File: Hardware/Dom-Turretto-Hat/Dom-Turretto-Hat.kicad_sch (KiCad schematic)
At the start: 12 parts, among them J1 Raspberry_Pi_2_3, U1 CAT24C32WI-GT3

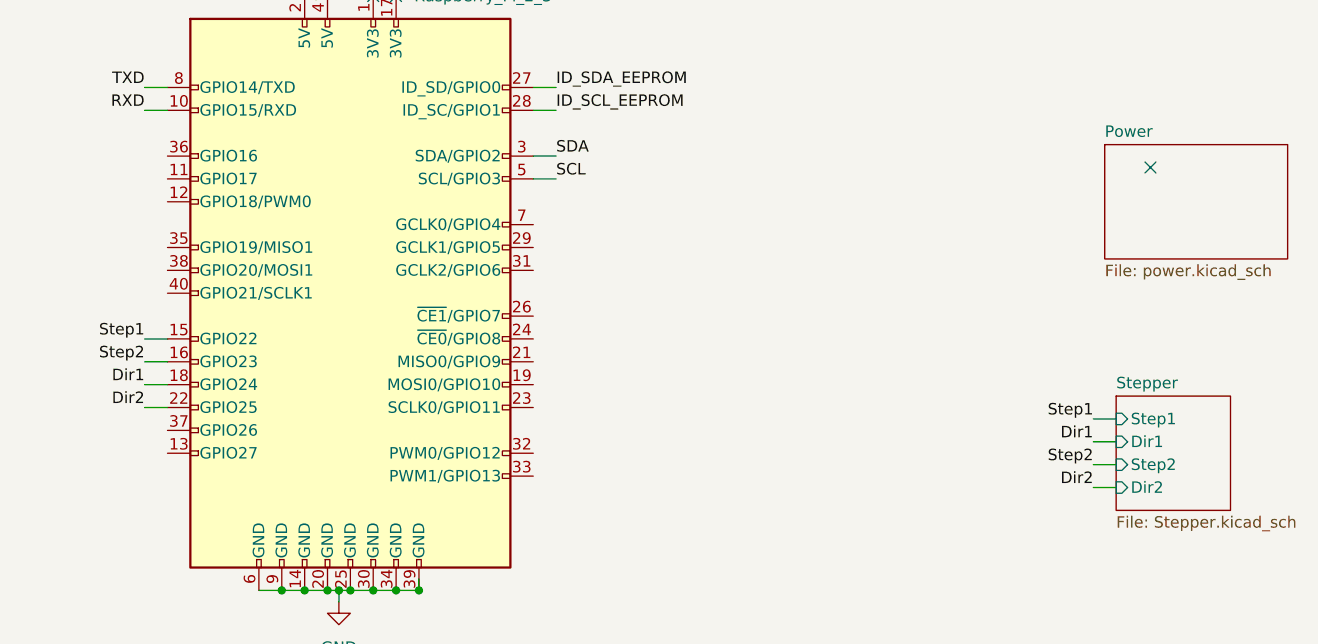
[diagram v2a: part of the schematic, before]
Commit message: Fix power circuitry values
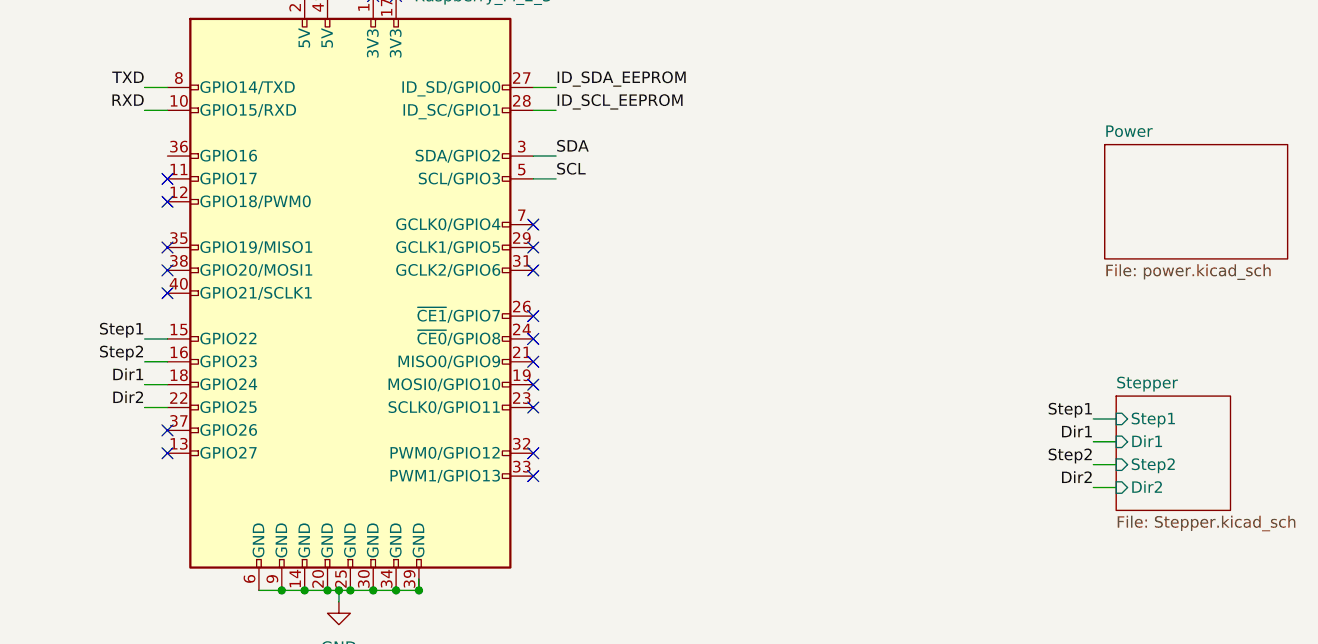
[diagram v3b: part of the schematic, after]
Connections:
- no-connect marks 4 -> 20
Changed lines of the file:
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@@
   (no_connect (at 146.05 69.85))
   (no_connect (at 148.59 69.85))
+  (no_connect (at 123.19 90.17))
+  (no_connect (at 123.19 100.33))
+  (no_connect (at 123.19 97.79))
+  (no_connect (at 123.19 92.71))
+  (no_connect (at 163.83 95.25))
+  (no_connect (at 163.83 97.79))
+  (no_connect (at 163.83 100.33))
+  (no_connect (at 163.83 105.41))
+  (no_connect (at 163.83 107.95))
+  (no_connect (at 163.83 110.49))
+  (no_connect (at 163.83 113.03))
+  (no_connect (at 163.83 115.57))
+  (no_connect (at 163.83 120.65))
+  (no_connect (at 163.83 123.19))
+  (no_connect (at 123.19 102.87))
+  (no_connect (at 123.19 120.65))
+  (no_connect (at 123.19 118.11))
   (no_connect (at -303.53 -21.59))
-  (no_connect (at 232.41 88.9))
   (wire (pts (xy 52.07 105.41) (xy 52.07 107.95))
     (stroke (width 0) (type default) (color 0 0 0 0))
@@
       (reference "#PWR013") (unit 1) (value "VCC") (footprint "")
     )
-    (path "/12e93b0c-a239-457f-b141-0c3b73a9b90a/4ae1d417-485a-437f-8fe9-cf7ad21c0f01"
-      (reference "#PWR014") (unit 1) (value "GND") (footprint "")
-    )
     (path "/12e93b0c-a239-457f-b141-0c3b73a9b90a/3dfc33ce-2f23-4a0c-8f41-0134d6c7a2a4"
       (reference "#PWR015") (unit 1) (value "GND") (footprint "")
@@
       (reference "#PWR021") (unit 1) (value "GND") (footprint "")
     )
-    (path "/12e93b0c-a239-457f-b141-0c3b73a9b90a/edde2f9a-acc0-48b1-bb93-b02152a9c39d"
-      (reference "#PWR026") (unit 1) (value "VCC") (footprint "")
-    )
     (path "/12e93b0c-a239-457f-b141-0c3b73a9b90a/23a39806-5bcf-46b3-9dd9-56270df61814"
       (reference "#PWR027") (unit 1) (value "GND") (footprint "")
@@
       (reference "#PWR0102") (unit 1) (value "GND") (footprint "")
     )
-    (path "/28fd1fbc-026b-4dd2-b303-4aef81adb474/a67e1f19-66f8-4d89-a414-1dd966045ad0"
-      (reference "#PWR0103") (unit 1) (value "+5V") (footprint "")
-    )
-    (path "/28fd1fbc-026b-4dd2-b303-4aef81adb474/9dc995cd-8c94-45d3-a4e1-d727a2822c72"
-      (reference "#PWR0104") (unit 1) (value "+5V") (footprint "")
-    )
-    (path "/28fd1fbc-026b-4dd2-b303-4aef81adb474/26251c45-5edc-47f5-bbe9-a3fa40eb07cf"
-      (reference "#PWR0105") (unit 1) (value "+5V") (footprint "")
-    )
-    (path "/28fd1fbc-026b-4dd2-b303-4aef81adb474/b601569f-09f4-4cef-b542-0b3745596966"
-      (reference "#PWR0106") (unit 1) (value "+5V") (footprint "")
-    )
-    (path "/28fd1fbc-026b-4dd2-b303-4aef81adb474/a83d4d91-ae71-431a-9357-40ec7588a902"
-      (reference "#PWR0107") (unit 1) (value "+5V") (footprint "")
-    )
-    (path "/28fd1fbc-026b-4dd2-b303-4aef81adb474/6788054c-34eb-4edd-af0a-8aff4765f859"
-      (reference "#PWR0108") (unit 1) (value "+5V") (footprint "")
-    )
-    (path "/28fd1fbc-026b-4dd2-b303-4aef81adb474/e9bf3fe6-e1cc-4b8d-bbb8-700e183aad7b"
-      (reference "#PWR0109") (unit 1) (value "+5V") (footprint "")
-    )
-    (path "/28fd1fbc-026b-4dd2-b303-4aef81adb474/35f07658-fb63-46ec-8bc3-dc98eda80c44"
-      (reference "#PWR0110") (unit 1) (value "+5V") (footprint "")
+    (path "/28fd1fbc-026b-4dd2-b303-4aef81adb474/c26481a5-551f-455c-a702-bce8abb1fe4e"
+      (reference "#PWR0103") (unit 1) (value "+3V3") (footprint "")
+    )
+    (path "/28fd1fbc-026b-4dd2-b303-4aef81adb474/7b37127e-e11c-4058-9b9e-3ba186a4a412"
+      (reference "#PWR0104") (unit 1) (value "+3V3") (footprint "")
+    )
+    (path "/28fd1fbc-026b-4dd2-b303-4aef81adb474/539ce550-73e1-4bff-bfe2-8c24d3e902a4"
+      (reference "#PWR0105") (unit 1) (value "+3V3") (footprint "")
+    )
+    (path "/28fd1fbc-026b-4dd2-b303-4aef81adb474/ae68f93a-eb13-4a21-940c-82130d925b20"
+      (reference "#PWR0106") (unit 1) (value "+3V3") (footprint "")
+    )
+    (path "/28fd1fbc-026b-4dd2-b303-4aef81adb474/3d9c11c1-d596-4401-a1a7-1c7f6241df8c"
+      (reference "#PWR0107") (unit 1) (value "+3V3") (footprint "")
+    )
+    (path "/28fd1fbc-026b-4dd2-b303-4aef81adb474/fa48996b-d3b8-4776-a72e-f75b7322c3d1"
+      (reference "#PWR0108") (unit 1) (value "+3V3") (footprint "")
+    )
+    (path "/28fd1fbc-026b-4dd2-b303-4aef81adb474/6521fb03-cbdb-41da-993d-d42db4a2d48a"
+      (reference "#PWR0109") (unit 1) (value "+3V3") (footprint "")
+    )
+    (path "/28fd1fbc-026b-4dd2-b303-4aef81adb474/5404de01-53f2-47e0-8e71-08810b932822"
+      (reference "#PWR0110") (unit 1) (value "+3V3") (footprint "")
+    )
+    (path "/12e93b0c-a239-457f-b141-0c3b73a9b90a/a639ca10-c811-4233-81c1-b214dc0c22a7"
+      (reference "#PWR0111") (unit 1) (value "GND") (footprint "")
     )
     (path "/28fd1fbc-026b-4dd2-b303-4aef81adb474/84977e32-dddb-4234-a567-e1e9c75d8f8b"
@@
       (reference "A2") (unit 1) (value "Pololu_Breakout_A4988") (footprint "Module:Pololu_Breakout-16_15.2x20.3mm")
     )
-    (path "/12e93b0c-a239-457f-b141-0c3b73a9b90a/ec276c8a-eb48-440f-b539-492777d28831"
-      (reference "C2") (unit 1) (value "22uF") (footprint "Capacitor_SMD:C_0603_1608Metric")
+    (path "/12e93b0c-a239-457f-b141-0c3b73a9b90a/4e526afd-8e77-485d-a370-3c86816ca539"
+      (reference "C1") (unit 1) (value "1uF") (footprint "Capacitor_SMD:C_0603_1608Metric")
+    )
+    (path "/12e93b0c-a239-457f-b141-0c3b73a9b90a/566f4d6a-3361-41fa-8a13-522c6df8e350"
+      (reference "C2") (unit 1) (value "10uF") (footprint "Capacitor_SMD:C_0603_1608Metric")
     )
     (path "/12e93b0c-a239-457f-b141-0c3b73a9b90a/ba2d8e02-8dff-41f2-94ab-2977ba7494f7"
-      (reference "C3") (unit 1) (value "6.8uF") (footprint "Capacitor_SMD:C_0603_1608Metric")
-    )
-    (path "/12e93b0c-a239-457f-b141-0c3b73a9b90a/881129b8-1053-44b9-bbe7-c43d6d8c66c3"
-      (reference "C4") (unit 1) (value "6.8uF") (footprint "Capacitor_SMD:C_0603_1608Metric")
+      (reference "C3") (unit 1) (value "10uF") (footprint "Capacitor_SMD:C_0603_1608Metric")
     )
     (path "/12e93b0c-a239-457f-b141-0c3b73a9b90a/f545c142-5d8e-40c4-b0fe-7c045a9cac0e"
@@
     )
     (path "/12e93b0c-a239-457f-b141-0c3b73a9b90a/70060f5d-b007-495f-a45f-7f1bfc4b8949"
-      (reference "C8") (unit 1) (value "180uF") (footprint "Capacitor_SMD:CP_Elec_8x11.9")
-    )
-    (path "/12e93b0c-a239-457f-b141-0c3b73a9b90a/24a04d23-1092-464e-96ea-d2d87b5f4b74"
-      (reference "C9") (unit 1) (value "10uF") (footprint "Capacitor_SMD:C_0603_1608Metric")
+      (reference "C8") (unit 1) (value "100uF") (footprint "Capacitor_SMD:CP_Elec_5x5.9")
     )
     (path "/12e93b0c-a239-457f-b141-0c3b73a9b90a/1e3bdcbd-8bf4-4d5f-8901-dadb4d9ff406"
@@
       (reference "C16") (unit 1) (value "47uF") (footprint "Capacitor_SMD:CP_Elec_6.3x7.7")
     )
-    (path "/12e93b0c-a239-457f-b141-0c3b73a9b90a/8a6cabaa-212f-4145-a004-b1da07d438ec"
-      (reference "D1") (unit 1) (value "D_Schottky") (footprint "Diode_SMD:D_SOD-123")
+    (path "/12e93b0c-a239-457f-b141-0c3b73a9b90a/b0d1c150-c935-43cc-9315-d503e1061c99"
+      (reference "C?") (unit 1) (value "47uF") (footprint "Capacitor_SMD:CP_Elec_6.3x7.7")
+    )
+    (path "/12e93b0c-a239-457f-b141-0c3b73a9b90a/23f8c4a1-bb0a-4aed-9a81-c18985f1140f"
+      (reference "D1") (unit 1) (value "DST1550S") (footprint "Package_TO_SOT_SMD:TO-277B")
     )
     (path "/12e93b0c-a239-457f-b141-0c3b73a9b90a/20d61a98-9d76-48c3-aea7-5d687e7dcd59"
@@
     )
     (path "/12e93b0c-a239-457f-b141-0c3b73a9b90a/89b193d6-28e4-4647-a3aa-6b8779163e05"
-      (reference "L2") (unit 1) (value "29uH") (footprint "Inductor_SMD:L_12x12mm_H8mm")
+      (reference "L2") (unit 1) (value "8.2uH") (footprint "iclr:Bourns_SRP1270")
     )
     (path "/12e93b0c-a239-457f-b141-0c3b73a9b90a/53065c22-5d58-4a1d-924c-019ba026a13b"
       (reference "PI_POW1") (unit 1) (value "LED") (footprint "LED_SMD:LED_0603_1608Metric")
     )
-    (path "/12e93b0c-a239-457f-b141-0c3b73a9b90a/87939eb2-1100-49c2-9486-7d16102560a9"
-      (reference "Q1") (unit 1) (value "RSJ250P10TL") (footprint "Package_TO_SOT_SMD:TO-263-3_TabPin2")
-    )
-    (path "/12e93b0c-a239-457f-b141-0c3b73a9b90a/d771511f-d16d-4f8b-8935-04481cf37b67"
-      (reference "Q2") (unit 1) (value "RSJ250P10TL") (footprint "Package_TO_SOT_SMD:TO-263-3_TabPin2")
+    (path "/12e93b0c-a239-457f-b141-0c3b73a9b90a/5a474f79-f8bc-4b50-af65-c0eaec3f07c2"
+      (reference "Q1") (unit 1) (value "SI4143DY-T1-GE3") (footprint "Package_SO:SOIC-8_3.9x4.9mm_P1.27mm")
+    )
+    (path "/12e93b0c-a239-457f-b141-0c3b73a9b90a/04240397-6670-4dea-a67c-9edaf7dd27dd"
+      (reference "Q2") (unit 1) (value "SI4143DY-T1-GE3") (footprint "Package_SO:SOIC-8_3.9x4.9mm_P1.27mm")
     )
     (path "/e3cbd370-7c22-4222-878e-9ad9b35baaf2"

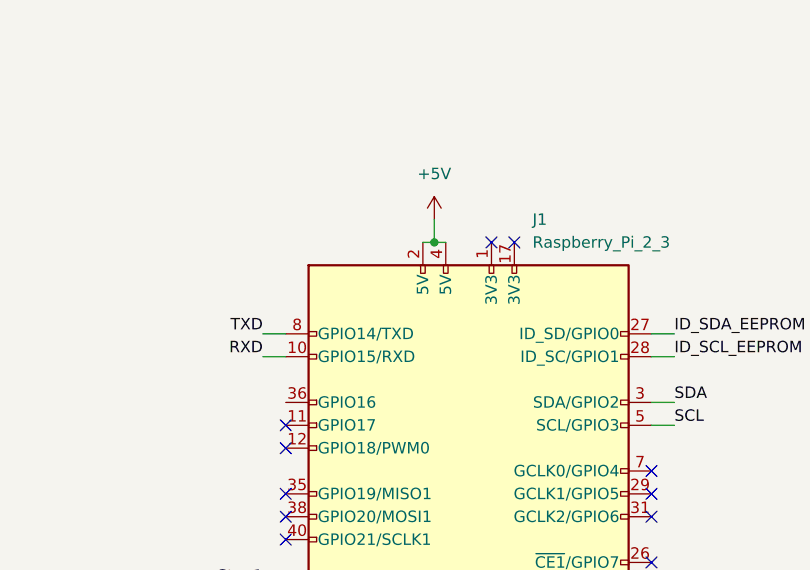
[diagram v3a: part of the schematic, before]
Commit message: Remove 3.3V regulator and use pi power for logic
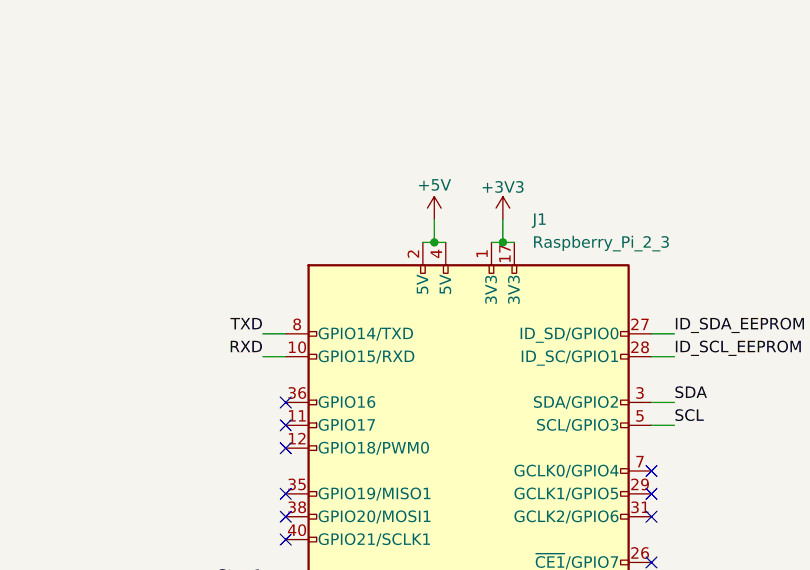
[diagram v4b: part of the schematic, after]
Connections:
- net +3V3: now also J1.1 (3V3), J1.17 (3V3)
- no-connect marks 20 -> 19

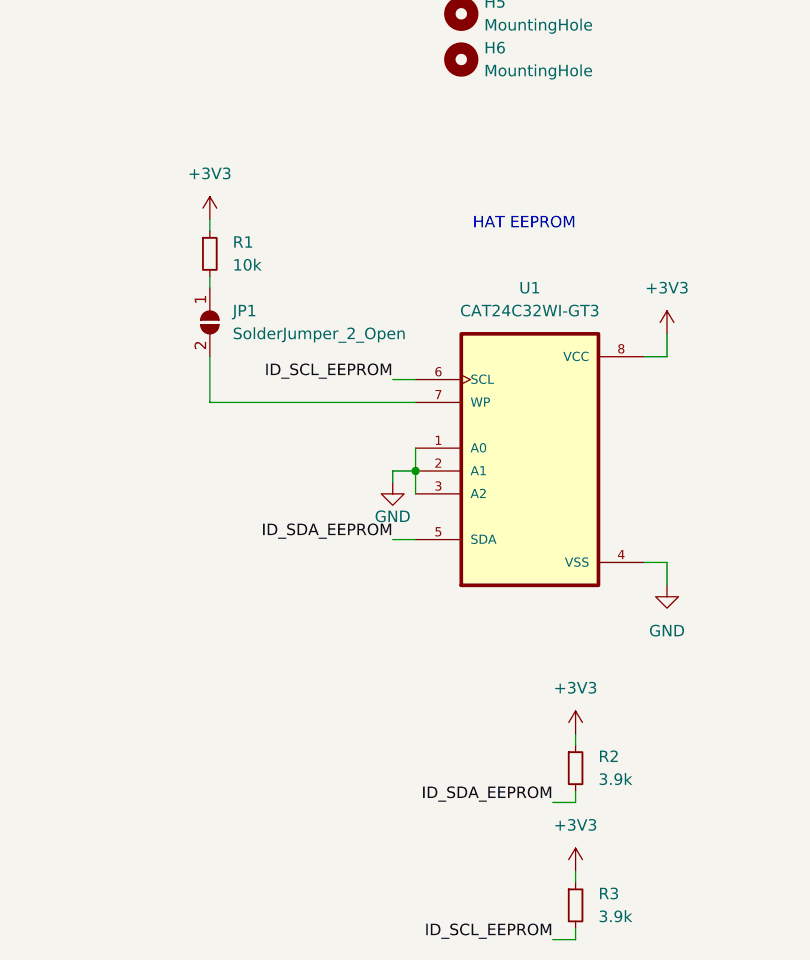
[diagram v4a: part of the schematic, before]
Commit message: Did initial laying out of components
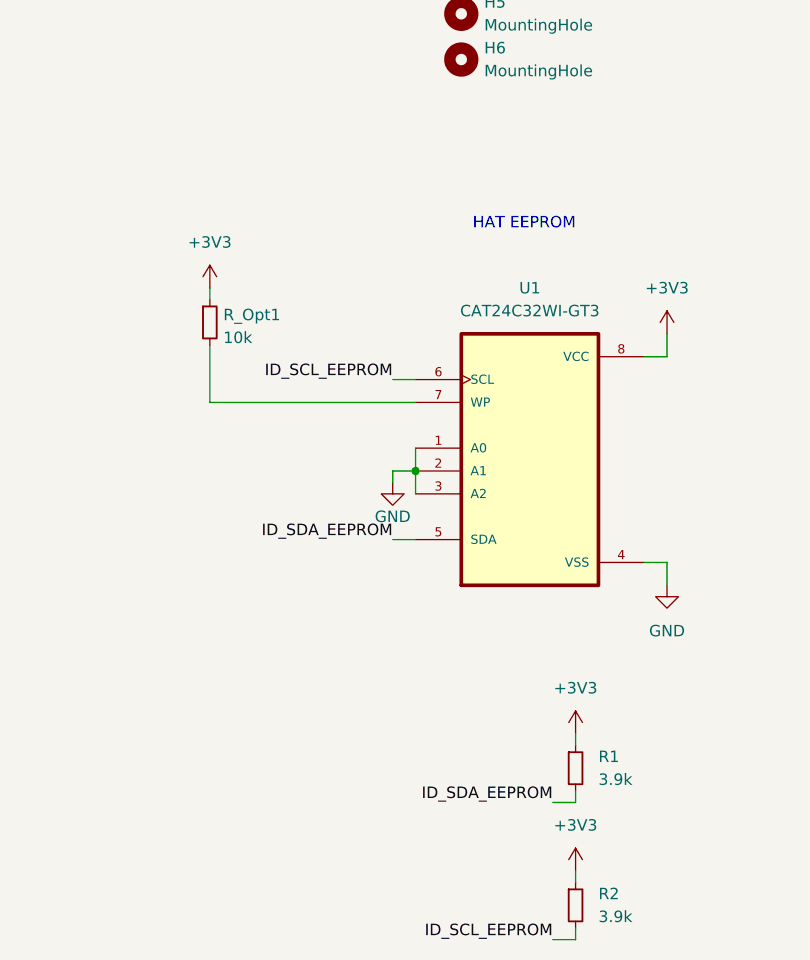
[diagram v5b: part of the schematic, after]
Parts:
- removed JP1: SolderJumper_2_Open, Jumper:SolderJumper-2_P1.3mm_Open_RoundedPad1.0x1.5mm, symbol Jumper:SolderJumper_2_Open
- renumbered R2 to R1, R3 to R2, R1 to R_Opt1
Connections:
- net at U1.7 (WP): now also R_Opt1.2
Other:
- moved on the sheet: R_Opt1

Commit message: Made better
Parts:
- added TP1: Step1, TestPoint:TestPoint_Pad_1.5x1.5mm, symbol Connector:TestPoint
- added TP2: Step2, TestPoint:TestPoint_Pad_1.5x1.5mm, symbol Connector:TestPoint
- added TP3: Dir1, TestPoint:TestPoint_Pad_1.5x1.5mm, symbol Connector:TestPoint
- added TP4: Dir2, TestPoint:TestPoint_Pad_1.5x1.5mm, symbol Connector:TestPoint
- added TP5: SDA_EEPROM, TestPoint:TestPoint_Pad_1.5x1.5mm, symbol Connector:TestPoint
- added TP6: SCL_EEPROM, TestPoint:TestPoint_Pad_1.5x1.5mm, symbol Connector:TestPoint
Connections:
- net Dir1: now also TP3.1
- net Dir2: now also TP4.1
- net ID_SCL_EEPROM: now also TP6.1
- net ID_SDA_EEPROM: now also TP5.1
- net Step1: now also TP1.1
- net Step2: now also TP2.1
- net RXD: no longer names the net of J1.10 (GPIO15/RXD)
- net SCL: no longer names the net of J1.5 (SCL/GPIO3)
- net SDA: no longer names the net of J1.3 (SDA/GPIO2)
- net TXD: no longer names the net of J1.8 (GPIO14/TXD)
- no-connect marks 19 -> 23
